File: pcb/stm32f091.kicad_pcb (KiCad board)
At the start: 2 copper layers, 63.5 x 38.2 mm, 42 parts, among them J3 Conn_02x05_Odd_Even, J4 Conn_02x03_Odd_Even, J5 Conn_02x03_Odd_Even, SW1 SW_Push, U1 LD1117S33TR_SOT223, U2 STM32F091RCTx, X1 32.768kHz(12.5pF), X2 8MHz(20pF)

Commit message: schematic complete
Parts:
- removed J4, J5: Conn_02x03_Odd_Even, Connector_PinHeader_1.27mm:PinHeader_2x03_P1.27mm_Vertical
- removed LD3: LED_Blue, LED_SMD:LED_0805_2012Metric
- removed LD4: LED_Green, LED_SMD:LED_0805_2012Metric
- removed LD5: LED_Yellow, LED_SMD:LED_0805_2012Metric
- removed LD6: LED_Red, LED_SMD:LED_0805_2012Metric
- removed R6: 3k, Resistor_SMD:R_0805_2012Metric_Pad1.15x1.40mm_HandSolder
- removed R7: 2k, Resistor_SMD:R_0805_2012Metric_Pad1.15x1.40mm_HandSolder
- removed R8: 1k, Resistor_SMD:R_0805_2012Metric_Pad1.15x1.40mm_HandSolder
- removed R9: 510, Resistor_SMD:R_0805_2012Metric_Pad1.15x1.40mm_HandSolder
- added C10: 1uF, Capacitor_SMD:C_0805_2012Metric_Pad1.15x1.40mm_HandSolder, F.Cu at (44.3, 67.8)
- added C16: 10uF, Capacitor_SMD:C_0805_2012Metric_Pad1.15x1.40mm_HandSolder, F.Cu at (44.3, 70.7)
- added C17: 10uF, Capacitor_SMD:C_0805_2012Metric_Pad1.15x1.40mm_HandSolder, F.Cu at (53.6, 67.3)
- added C18: 10uF, Capacitor_SMD:C_0805_2012Metric_Pad1.15x1.40mm_HandSolder, F.Cu at (49.0, 70.2)
- added C19: 10uF, Capacitor_SMD:C_0805_2012Metric_Pad1.15x1.40mm_HandSolder, F.Cu at (53.8, 70.2)
- added C20: 0.1uF, Capacitor_SMD:C_0805_2012Metric_Pad1.15x1.40mm_HandSolder, F.Cu at (58.5, 67.3)
- added C21: 0.1uF, Capacitor_SMD:C_0805_2012Metric_Pad1.15x1.40mm_HandSolder, F.Cu at (63.3, 67.3)
- added D3: BAT60JFILM, Diode_SMD:D_SOD-323, F.Cu at (58.3, 70.2)
- added J1: USB_B_Micro, Connector_USB:USB_Micro-B_Molex_47346-0001, F.Cu at (73.6, 64.4)
- added J10: Touch, Connector_PinHeader_2.54mm:PinHeader_1x04_P2.54mm_Vertical, F.Cu at (80.0, 51.3)
- added J2: Audio, Connector_PinSocket_2.54mm:PinSocket_1x04_P2.54mm_Vertical, F.Cu at (70.7, 51.3)
- added J6: UART, Connector_PinHeader_2.54mm:PinHeader_1x06_P2.54mm_Vertical, F.Cu at (44.2, 51.3)
- added J7: Micro_SD_Card, Connector_Card:microSD_HC_Wuerth_693072010801, F.Cu at (59.8, 56.8)
- added J8: LCD, Connector_PinHeader_2.54mm:PinHeader_1x06_P2.54mm_Vertical, F.Cu at (48.9, 51.3)
- added J9: Keypad, Connector_PinHeader_2.54mm:PinHeader_1x04_P2.54mm_Vertical, F.Cu at (75.3, 51.3)
- R4, R5: value 1k -> 470
- moved R11 37.8 mm to (106.6, 76.7), turned to 0 degrees
- moved X1 34.5 mm to (115.8, 77.5)
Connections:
- C12 pad 1: Net-(C12-Pad1) -> /PC14
- C13 pad 1: Net-(C13-Pad1) -> /PC15
- C14 pad 1: Net-(C14-Pad1) -> /PF0
- D1 pad 2: /U5V -> Net-(D1-Pad2)
- J3 pad 10: /U5V -> (no net)
- J3 pad 5: Net-(J3-Pad5) -> (no net)
- J3 pad 9: /U5V -> (no net)
- R11 pad 1: Net-(J5-Pad6) -> /PF1
- R4 pad 1: /PA0 -> /I2C_SCL
- R4 pad 2: Net-(R4-Pad2) -> +3V0
- R5 pad 1: /PB2 -> +3V0
- R5 pad 2: Net-(R5-Pad2) -> /I2C_SDA
- U1 pad 1: GND -> Net-(D3-Pad2)
- U2 pad 10: /PC2 -> /SD_SPI_MISO
- U2 pad 11: /PC3 -> /SD_SPI_MOSI
- U2 pad 2: /PC13 -> (no net)
- U2 pad 20: /PA4 -> /DAC
- U2 pad 21: /PA5 -> (no net)
- U2 pad 22: /PA6 -> (no net)
- U2 pad 23: /PA7 -> (no net)
- U2 pad 24: /PC4 -> (no net)
- U2 pad 25: /PC5 -> (no net)
- U2 pad 26: /PB0 -> (no net)
- U2 pad 27: /PB1 -> (no net)
- U2 pad 28: /PB2 -> (no net)
- U2 pad 29: /PB10 -> (no net)
- U2 pad 30: /PB11 -> (no net)
- U2 pad 33: /PB12 -> /SD_SPI_CS
- U2 pad 34: /PB13 -> /SD_SPI_CLK
- U2 pad 35: /PB14 -> /LCD_DC
- U2 pad 36: /PB15 -> (no net)
- U2 pad 37: /PC6 -> (no net)
- U2 pad 38: /PC7 -> (no net)
- U2 pad 39: /PC8 -> (no net)
- U2 pad 40: /PC9 -> (no net)
- U2 pad 41: /PA8 -> (no net)
- U2 pad 42: /PA9 -> (no net)
- U2 pad 43: /PA10 -> (no net)
- U2 pad 44: /PA11 -> (no net)
- U2 pad 45: /PA12 -> (no net)
- U2 pad 50: /PA15 -> (no net)
- U2 pad 51: /PC10 -> (no net)
- U2 pad 52: /PC11 -> (no net)
- U2 pad 56: /PB4 -> (no net)
- U2 pad 58: /PB6 -> /I2C_SCL
- U2 pad 59: /PB7 -> /I2C_SDA
- U2 pad 62: /PB9 -> (no net)
- U2 pad 8: /PC0 -> (no net)
- U2 pad 9: /PC1 -> (no net)
- X1 pad 1: Net-(C12-Pad1) -> /PC14
- X1 pad 2: Net-(C13-Pad1) -> /PC15
- X2 pad 1: Net-(C14-Pad1) -> /PF0

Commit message: Board Layout
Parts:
- R11: moved to B.Cu
- moved C8 63.0 mm to (94.5, 117.3)
- moved R5 62.3 mm to (93.4, 85.9)
- moved J6 61.3 mm to (88.3, 93.9), turned to 90 degrees
- moved J7 60.8 mm to (69.9, 116.8)
- moved R4 59.3 mm to (106.7, 115.5)
- moved J10 49.4 mm to (90.2, 99.6), turned to 270 degrees
- moved J2 42.8 mm to (75.8, 93.8)
- moved C6 41.4 mm to (109.2, 111.7)
- moved C10 39.3 mm to (71.1, 96.4), turned to 180 degrees
- moved J3 37.0 mm to (113.0, 78.7)
- moved C1 36.3 mm to (112.0, 86.3)
- moved C3 36.3 mm to (115.9, 86.3)
- moved D1 36.2 mm to (105.4, 86.3), turned to 180 degrees
- moved C4 35.6 mm to (112.1, 96.8)
- moved D2 35.6 mm to (116.3, 96.8)
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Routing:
- net +3V0: track 0.00 -> 140.4 mm, vias 0 -> 10
- net +5V: track 0.00 -> 86.2 mm, vias 0 -> 2
- net /LCD_DC: track 0.00 -> 55.9 mm, vias 0 -> 2
- net /I2C_SCL: track 0.00 -> 51.5 mm, vias 0 -> 3
- net GND: track 0.00 -> 50.8 mm, vias 0 -> 8
- net /NRST: track 0.00 -> 50.7 mm, vias 0 -> 2
- net /PB5: track 0.00 -> 50.0 mm, vias 0 -> 4
- net /PB3: track 0.00 -> 47.6 mm, vias 0 -> 3
- net /SD_SPI_CS: track 0.00 -> 46.7 mm
- net /PA13: track 0.00 -> 46.0 mm, vias 0 -> 1
- net /PB8: track 0.00 -> 44.1 mm, vias 0 -> 3
- net /I2C_SDA: track 0.00 -> 38.2 mm, vias 0 -> 5
- net /PC14: track 0.00 -> 35.7 mm, vias 0 -> 2
- net /DAC: track 0.00 -> 33.3 mm, vias 0 -> 4
- net /SD_SPI_CLK: track 0.00 -> 32.6 mm, vias 0 -> 2
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- added copper zone on F.Cu, net GND
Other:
- board size 63.5 x 38.2 mm -> 63.5 x 50.8 mm

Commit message: completed pcb
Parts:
- added MOUNT: MountingHole_3.2mm_M3, MountingHole:MountingHole_3.2mm_M3, F.Cu at (121.3, 122.5)
- added MOUNT: MountingHole_3.2mm_M3, MountingHole:MountingHole_3.2mm_M3, F.Cu at (64.2, 122.5)
- J3: value Conn_02x05_Odd_Even -> PRG
- moved R4 32.0 mm to (93.4, 86.4), turned to 0 degrees
- moved D3 30.1 mm to (117.0, 94.1), turned to 180 degrees
- moved J8 21.1 mm to (76.0, 95.9), turned to 180 degrees
- moved C6 15.6 mm to (96.7, 102.5), turned to 45 degrees
- moved J2 14.9 mm to (70.4, 107.7), turned to 270 degrees
- moved D1 14.0 mm to (92.4, 81.2)
- moved C18 13.2 mm to (79.0, 94.9), turned to 270 degrees
- moved C10 10.9 mm to (74.3, 106.9), turned to 0 degrees
- moved C17 10.4 mm to (77.3, 80.0), turned to 180 degrees
- moved C16 10.3 mm to (72.8, 95.1), turned to 270 degrees
- moved C19 10.3 mm to (81.3, 80.0)
- moved J7 8.06 mm to (77.8, 118.4), turned to 180 degrees
- moved C21 6.78 mm to (85.1, 84.1), turned to 180 degrees
- moved C20 6.00 mm to (73.2, 89.9), turned to 90 degrees
- moved R5 2.16 mm to (92.0, 84.2), turned to 180 degrees
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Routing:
- net GND: track 50.8 -> 19.4 mm, vias 8 -> 106
- net Net-(D3-Pad2): track 29.4 -> 2.62 mm, vias 2 -> 0
- net /SD_SPI_CS: track 46.7 -> 26.8 mm
- net Net-(D1-Pad2): track 18.9 -> 2.66 mm
- net /PB5: track 50.0 -> 35.6 mm, vias 4 -> 2
- net /I2C_SCL: track 51.5 -> 37.3 mm, vias 3 -> 1
- net /DAC: track 33.3 -> 20.9 mm, vias 4 -> 2
- net /LCD_DC: track 55.9 -> 45.4 mm, vias 2 -> 1
- net /NRST: track 50.7 -> 60.9 mm, vias 2 -> 1
- net +3V0: track 140.4 -> 130.2 mm, vias 10 -> 7
- net /PB8: track 44.1 -> 37.7 mm, vias 3 -> 2
- net /SD_SPI_MISO: track 27.7 -> 32.9 mm, vias 2 -> 0
- net /I2C_SDA: track 38.2 -> 41.4 mm
- net /PC14: track 35.7 -> 32.7 mm
- net /PB3: track 47.6 -> 44.8 mm, vias 3 -> 2
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
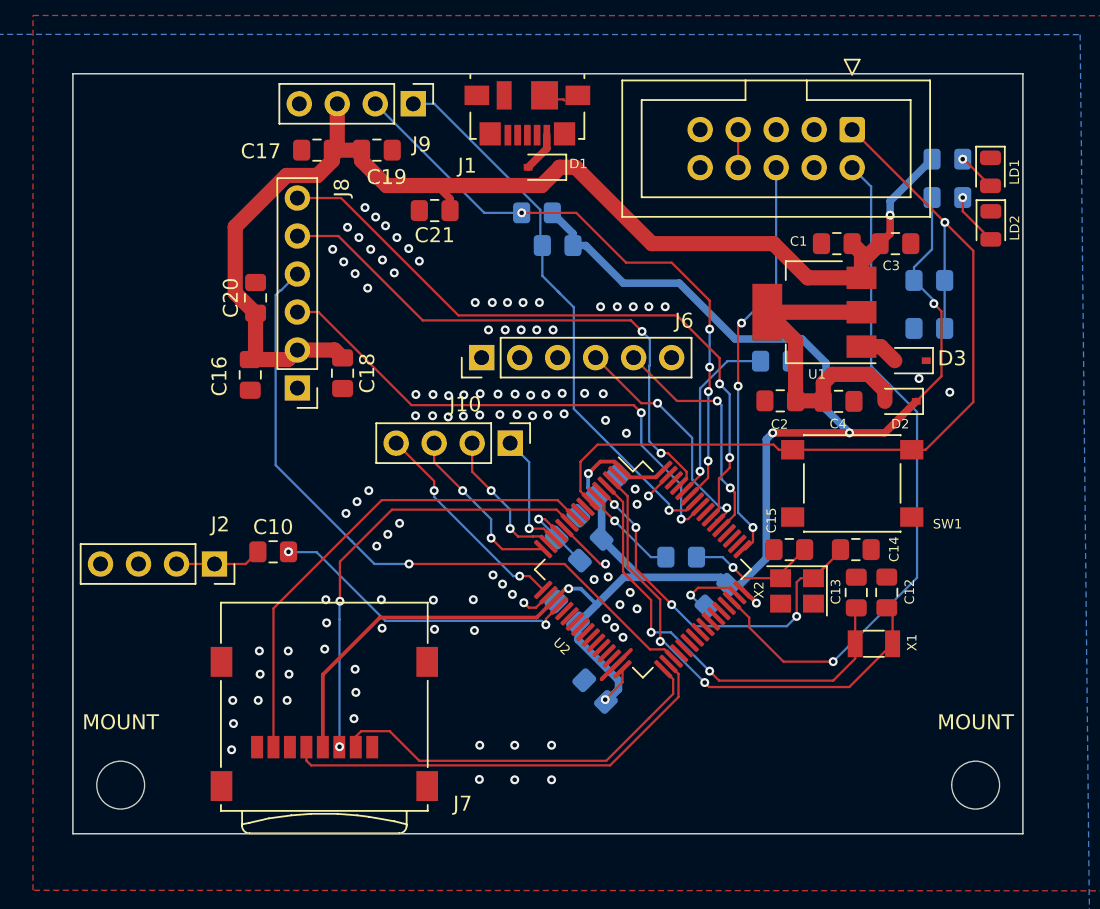
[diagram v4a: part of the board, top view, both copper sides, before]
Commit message: stitched vias
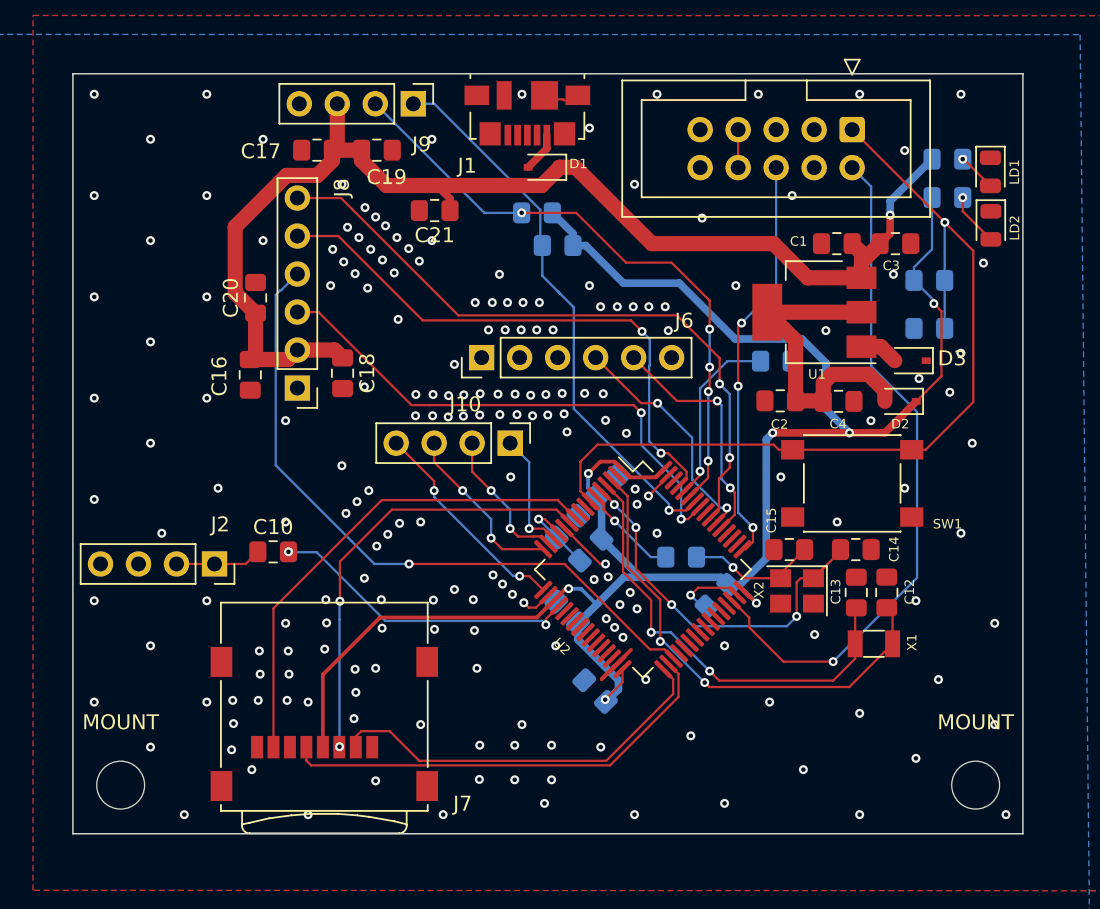
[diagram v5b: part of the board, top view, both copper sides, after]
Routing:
- net GND: vias 106 -> 199
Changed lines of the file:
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@@
     (thickness 1.6)
     (drawings 6)
-    (tracks 557)
+    (tracks 650)
     (zones 0)
     (modules 49)
@@
   (via (at 81.27222 106.50316) (size 0.6) (drill 0.3) (layers F.Cu B.Cu) (net 1))
   (via (at 82.79622 104.97916) (size 0.6) (drill 0.3) (layers F.Cu B.Cu) (net 1))
+  (via (at 62.38642 76.298771) (size 0.6) (drill 0.3) (layers F.Cu B.Cu) (net 1))
+  (via (at 62.38642 83.070371) (size 0.6) (drill 0.3) (layers F.Cu B.Cu) (net 1))
+  (via (at 62.38642 89.841971) (size 0.6) (drill 0.3) (layers F.Cu B.Cu) (net 1))
+  (via (at 62.38642 96.613571) (size 0.6) (drill 0.3) (layers F.Cu B.Cu) (net 1))
+  (via (at 62.38642 103.385171) (size 0.6) (drill 0.3) (layers F.Cu B.Cu) (net 1))
+  (via (at 62.38642 110.156771) (size 0.6) (drill 0.3) (layers F.Cu B.Cu) (net 1))
+  (via (at 62.38642 116.928371) (size 0.6) (drill 0.3) (layers F.Cu B.Cu) (net 1))
+  (via (at 66.14842 79.308371) (size 0.6) (drill 0.3) (layers F.Cu B.Cu) (net 1))
+  (via (at 66.14842 86.079971) (size 0.6) (drill 0.3) (layers F.Cu B.Cu) (net 1))
+  (via (at 66.14842 92.851571) (size 0.6) (drill 0.3) (layers F.Cu B.Cu) (net 1))
+  (via (at 66.14842 99.623171) (size 0.6) (drill 0.3) (layers F.Cu B.Cu) (net 1))
+  (via (at 66.14842 113.166371) (size 0.6) (drill 0.3) (layers F.Cu B.Cu) (net 1))
+  (via (at 66.14842 119.937971) (size 0.6) (drill 0.3) (layers F.Cu B.Cu) (net 1))
+  (via (at 66.90082 105.642371) (size 0.6) (drill 0.3) (layers F.Cu B.Cu) (net 1))
+  (via (at 68.40562 124.452371) (size 0.6) (drill 0.3) (layers F.Cu B.Cu) (net 1))
+  (via (at 69.91042 76.298771) (size 0.6) (drill 0.3) (layers F.Cu B.Cu) (net 1))
+  (via (at 69.91042 83.070371) (size 0.6) (drill 0.3) (layers F.Cu B.Cu) (net 1))
+  (via (at 69.91042 89.841971) (size 0.6) (drill 0.3) (layers F.Cu B.Cu) (net 1))
+  (via (at 69.91042 96.613571) (size 0.6) (drill 0.3) (layers F.Cu B.Cu) (net 1))
+  (via (at 69.91042 110.156771) (size 0.6) (drill 0.3) (layers F.Cu B.Cu) (net 1))
+  (via (at 69.91042 116.928371) (size 0.6) (drill 0.3) (layers F.Cu B.Cu) (net 1))
+  (via (at 70.66282 102.632771) (size 0.6) (drill 0.3) (layers F.Cu B.Cu) (net 1))
+  (via (at 72.92002 121.442771) (size 0.6) (drill 0.3) (layers F.Cu B.Cu) (net 1))
+  (via (at 73.67242 79.308371) (size 0.6) (drill 0.3) (layers F.Cu B.Cu) (net 1))
+  (via (at 73.67242 86.079971) (size 0.6) (drill 0.3) (layers F.Cu B.Cu) (net 1))
+  (via (at 75.17722 98.118371) (size 0.6) (drill 0.3) (layers F.Cu B.Cu) (net 1))
+  (via (at 75.17722 104.889971) (size 0.6) (drill 0.3) (layers F.Cu B.Cu) (net 1))
+  (via (at 75.17722 111.661571) (size 0.6) (drill 0.3) (layers F.Cu B.Cu) (net 1))
+  (via (at 76.68202 116.928371) (size 0.6) (drill 0.3) (layers F.Cu B.Cu) (net 1))
+  (via (at 76.68202 124.452371) (size 0.6) (drill 0.3) (layers F.Cu B.Cu) (net 1))
+  (via (at 78.18682 89.089571) (size 0.6) (drill 0.3) (layers F.Cu B.Cu) (net 1))
+  (via (at 78.93922 82.317971) (size 0.6) (drill 0.3) (layers F.Cu B.Cu) (net 1))
+  (via (at 78.93922 101.127971) (size 0.6) (drill 0.3) (layers F.Cu B.Cu) (net 1))
+  (via (at 80.44402 95.861171) (size 0.6) (drill 0.3) (layers F.Cu B.Cu) (net 1))
+  (via (at 80.44402 108.651971) (size 0.6) (drill 0.3) (layers F.Cu B.Cu) (net 1))
+  (via (at 81.19642 114.671171) (size 0.6) (drill 0.3) (layers F.Cu B.Cu) (net 1))
+  (via (at 81.19642 122.195171) (size 0.6) (drill 0.3) (layers F.Cu B.Cu) (net 1))
+  (via (at 82.70122 91.346771) (size 0.6) (drill 0.3) (layers F.Cu B.Cu) (net 1))
+  (via (at 84.20602 104.889971) (size 0.6) (drill 0.3) (layers F.Cu B.Cu) (net 1))
+  (via (at 84.20602 118.433171) (size 0.6) (drill 0.3) (layers F.Cu B.Cu) (net 1))
+  (via (at 84.95842 79.308371) (size 0.6) (drill 0.3) (layers F.Cu B.Cu) (net 1))
+  (via (at 84.95842 86.079971) (size 0.6) (drill 0.3) (layers F.Cu B.Cu) (net 1))
+  (via (at 85.71082 124.452371) (size 0.6) (drill 0.3) (layers F.Cu B.Cu) (net 1))
+  (via (at 86.46322 94.356371) (size 0.6) (drill 0.3) (layers F.Cu B.Cu) (net 1))
+  (via (at 86.46322 109.404371) (size 0.6) (drill 0.3) (layers F.Cu B.Cu) (net 1))
+  (via (at 87.96802 114.671171) (size 0.6) (drill 0.3) (layers F.Cu B.Cu) (net 1))
+  (via (at 89.47282 88.337171) (size 0.6) (drill 0.3) (layers F.Cu B.Cu) (net 1))
+  (via (at 90.22522 101.880371) (size 0.6) (drill 0.3) (layers F.Cu B.Cu) (net 1))
+  (via (at 90.97762 76.298771) (size 0.6) (drill 0.3) (layers F.Cu B.Cu) (net 1))
+  (via (at 90.97762 118.433171) (size 0.6) (drill 0.3) (layers F.Cu B.Cu) (net 1))
+  (via (at 92.48242 123.699971) (size 0.6) (drill 0.3) (layers F.Cu B.Cu) (net 1))
+  (via (at 93.23482 113.166371) (size 0.6) (drill 0.3) (layers F.Cu B.Cu) (net 1))
+  (via (at 93.98722 98.870771) (size 0.6) (drill 0.3) (layers F.Cu B.Cu) (net 1))
+  (via (at 95.49202 78.555971) (size 0.6) (drill 0.3) (layers F.Cu B.Cu) (net 1))
+  (via (at 95.49202 89.089571) (size 0.6) (drill 0.3) (layers F.Cu B.Cu) (net 1))
+  (via (at 96.24442 119.937971) (size 0.6) (drill 0.3) (layers F.Cu B.Cu) (net 1))
+  (via (at 98.50162 82.317971) (size 0.6) (drill 0.3) (layers F.Cu B.Cu) (net 1))
+  (via (at 98.50162 124.452371) (size 0.6) (drill 0.3) (layers F.Cu B.Cu) (net 1))
+  (via (at 99.25402 115.423571) (size 0.6) (drill 0.3) (layers F.Cu B.Cu) (net 1))
+  (via (at 100.00642 76.298771) (size 0.6) (drill 0.3) (layers F.Cu B.Cu) (net 1))
+  (via (at 100.00642 105.642371) (size 0.6) (drill 0.3) (layers F.Cu B.Cu) (net 1))
+  (via (at 100.75882 92.099171) (size 0.6) (drill 0.3) (layers F.Cu B.Cu) (net 1))
+  (via (at 102.26362 119.185571) (size 0.6) (drill 0.3) (layers F.Cu B.Cu) (net 1))
+  (via (at 103.01602 84.575171) (size 0.6) (drill 0.3) (layers F.Cu B.Cu) (net 1))
+  (via (at 104.52082 113.166371) (size 0.6) (drill 0.3) (layers F.Cu B.Cu) (net 1))
+  (via (at 104.52082 123.699971) (size 0.6) (drill 0.3) (layers F.Cu B.Cu) (net 1))
+  (via (at 105.27322 89.089571) (size 0.6) (drill 0.3) (layers F.Cu B.Cu) (net 1))
+  (via (at 106.77802 76.298771) (size 0.6) (drill 0.3) (layers F.Cu B.Cu) (net 1))
+  (via (at 107.53042 116.928371) (size 0.6) (drill 0.3) (layers F.Cu B.Cu) (net 1))
+  (via (at 108.28282 101.880371) (size 0.6) (drill 0.3) (layers F.Cu B.Cu) (net 1))
+  (via (at 109.03522 83.070371) (size 0.6) (drill 0.3) (layers F.Cu B.Cu) (net 1))
+  (via (at 109.78762 121.442771) (size 0.6) (drill 0.3) (layers F.Cu B.Cu) (net 1))
+  (via (at 110.54002 112.413971) (size 0.6) (drill 0.3) (layers F.Cu B.Cu) (net 1))
+  (via (at 111.29242 92.099171) (size 0.6) (drill 0.3) (layers F.Cu B.Cu) (net 1))
+  (via (at 112.04482 104.889971) (size 0.6) (drill 0.3) (layers F.Cu B.Cu) (net 1))
+  (via (at 113.54962 76.298771) (size 0.6) (drill 0.3) (layers F.Cu B.Cu) (net 1))
+  (via (at 113.54962 117.680771) (size 0.6) (drill 0.3) (layers F.Cu B.Cu) (net 1))
+  (via (at 113.54962 124.452371) (size 0.6) (drill 0.3) (layers F.Cu B.Cu) (net 1))
+  (via (at 114.30202 98.118371) (size 0.6) (drill 0.3) (layers F.Cu B.Cu) (net 1))
+  (via (at 115.80682 88.337171) (size 0.6) (drill 0.3) (layers F.Cu B.Cu) (net 1))
+  (via (at 116.55922 80.060771) (size 0.6) (drill 0.3) (layers F.Cu B.Cu) (net 1))
+  (via (at 116.55922 102.632771) (size 0.6) (drill 0.3) (layers F.Cu B.Cu) (net 1))
+  (via (at 117.31162 110.156771) (size 0.6) (drill 0.3) (layers F.Cu B.Cu) (net 1))
+  (via (at 117.31162 120.690371) (size 0.6) (drill 0.3) (layers F.Cu B.Cu) (net 1))
+  (via (at 118.81642 115.423571) (size 0.6) (drill 0.3) (layers F.Cu B.Cu) (net 1))
+  (via (at 120.32122 76.298771) (size 0.6) (drill 0.3) (layers F.Cu B.Cu) (net 1))
+  (via (at 120.32122 93.603971) (size 0.6) (drill 0.3) (layers F.Cu B.Cu) (net 1))
+  (via (at 120.32122 105.642371) (size 0.6) (drill 0.3) (layers F.Cu B.Cu) (net 1))
+  (via (at 121.07362 99.623171) (size 0.6) (drill 0.3) (layers F.Cu B.Cu) (net 1))
+  (via (at 121.82602 87.584771) (size 0.6) (drill 0.3) (layers F.Cu B.Cu) (net 1))
+  (via (at 122.57842 111.661571) (size 0.6) (drill 0.3) (layers F.Cu B.Cu) (net 1))
+  (via (at 122.57842 118.433171) (size 0.6) (drill 0.3) (layers F.Cu B.Cu) (net 1))
+  (via (at 123.33082 124.452371) (size 0.6) (drill 0.3) (layers F.Cu B.Cu) (net 1))
   (segment (start 118.38918 80.63738) (end 118.38918 80.9432) (width 0.1524) (layer B.Cu) (net 2))
   (segment (start 112.87181 86.46057) (end 113.04762 86.28476) (width 0.1524) (layer F.Cu) (net 2))
